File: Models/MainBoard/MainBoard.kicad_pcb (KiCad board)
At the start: 4 copper layers, 81 parts, among them J1 Conn_Coaxial, J10 Conn_01x04_Pin, J11 Conn_01x04_Pin, J12 Conn_01x04_Pin, J13 Conn_01x09_Pin, J14 Conn_01x13_Pin, J15 Conn_01x24_Socket, J18 Conn_01x24_Socket, J2 Conn_Coaxial, J3 Conn_Coaxial, J4 Conn_Coaxial, J5 Conn_Coaxial, J6 Conn_Coaxial, J7 Conn_01x04_Pin, J8 Conn_01x04_Pin, J9 Conn_01x04_Pin, U1 ADS8699, U2 AD7745, U3 DAC81404, U4 DAC81401, U5 ISO7761DW, U6 ISO1641DW

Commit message: Save progress
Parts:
- moved J2 23.4 mm to (70.8, 57.1)
- moved J1 12.3 mm to (53.5, 48.3)
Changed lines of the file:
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@@
 	(footprint "Connector_Custom:RFPC-SMA27-F"
 		(layer "F.Cu")
-		(at 53.98 60.66)
+		(at 53.48 48.34)
 		(property "Reference" "J1"
 			(at 0.415 -4.385 0)
@@
 			)
 		)
-		(property "Purchase Link" "https://www.digikey.com/en/products/detail/gct/RFPC-SMA27-F/22162144"
+		(property "Purchase Link" "https://www.digikey.com/en/products/detail/molex/0733660030/1465162"
 			(at 0 0 0)
 			(unlocked yes)
@@
 			)
 		)
-		(property "Cost" "$1.916"
+		(property "Cost" "$3.146"
 			(at 0 0 0)
 			(unlocked yes)
@@
 			)
 		)
-		(property "Purchase Link" "https://www.digikey.com/en/products/detail/gct/RFPC-SMA27-F/22162144"
+		(property "Purchase Link" "https://www.digikey.com/en/products/detail/molex/0733660030/1465162"
 			(at 0 0 0)
 			(unlocked yes)
@@
 			)
 		)
-		(property "Cost" "$1.916"
+		(property "Cost" "$3.146"
 			(at 0 0 0)
 			(unlocked yes)
@@
 			)
 		)
-		(property "Purchase Link" "https://www.digikey.com/en/products/detail/gct/RFPC-SMA27-F/22162144"
+		(property "Purchase Link" "https://www.digikey.com/en/products/detail/molex/0733660030/1465162"
 			(at 0 0 0)
 			(unlocked yes)
@@
 			)
 		)
-		(property "Cost" "$1.916"
+		(property "Cost" "$3.146"
 			(at 0 0 0)
 			(unlocked yes)
@@
 	(footprint "Connector_Custom:RFPC-SMA27-F"
 		(layer "F.Cu")
-		(at 53.98 73.36)
+		(at 70.78 57.08)
 		(property "Reference" "J2"
 			(at 0.415 -4.385 0)
@@
 			)
 		)
-		(property "Purchase Link" "https://www.digikey.com/en/products/detail/gct/RFPC-SMA27-F/22162144"
+		(property "Purchase Link" "https://www.digikey.com/en/products/detail/molex/0733660030/1465162"
 			(at 0 0 0)
 			(unlocked yes)
@@
 			)
 		)
-		(property "Cost" "$1.916"
+		(property "Cost" "$3.146"
 			(at 0 0 0)
 			(unlocked yes)
@@
 			)
 		)
-		(property "Purchase Link" "https://www.digikey.com/en/products/detail/gct/RFPC-SMA27-F/22162144"
+		(property "Purchase Link" "https://www.digikey.com/en/products/detail/molex/0733660030/1465162"
 			(at 0 0 0)
 			(unlocked yes)
@@
 			)
 		)
-		(property "Cost" "$1.916"
+		(property "Cost" "$3.146"
 			(at 0 0 0)
 			(unlocked yes)
@@
 			)
 		)
-		(property "Purchase Link" "https://www.digikey.com/en/products/detail/gct/RFPC-SMA27-F/22162144"
+		(property "Purchase Link" "https://www.digikey.com/en/products/detail/molex/0733660030/1465162"
 			(at 0 0 0)
 			(unlocked yes)
@@
 			)
 		)
-		(property "Cost" "$1.916"
+		(property "Cost" "$3.146"
 			(at 0 0 0)
 			(unlocked yes)

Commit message: Push uncommitted changes
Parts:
- J10, J11, J12, J7, J8, J9: value Conn_01x04_Pin -> Conn_01x03_Pin
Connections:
- J10 pad 3: /ADC_GND -> Net-(J10-Pin_3)
- J10 pad 4: Net-(J10-Pin_4) -> (no net)
- J11 pad 1: GND -> /CDC_EXC
- J11 pad 3: /CDC_EXC -> GND
- J11 pad 4: GND -> (no net)
- J12 pad 1: GND -> /CDC_CIN
- J12 pad 3: /CDC_CIN -> GND
- J12 pad 4: GND -> (no net)
- J7 pad 1: GND -> /BIAS_OUT
- J7 pad 3: /BIAS_OUT -> GND
- J7 pad 4: GND -> (no net)
- J8 pad 3: /BIAS_GND -> Net-(J8-Pin_3)
- J8 pad 4: Net-(J8-Pin_4) -> (no net)
- J9 pad 1: GND -> /ADC_IN
- J9 pad 3: /ADC_IN -> GND
- J9 pad 4: GND -> (no net)
- R1 pad 1: Net-(J8-Pin_4) -> Net-(J8-Pin_3)
- R2 pad 1: Net-(J10-Pin_4) -> Net-(J10-Pin_3)
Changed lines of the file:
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@@
 	(net 26 "/CDC_EXC")
 	(net 27 "/CDC_CIN")
-	(net 28 "Net-(J8-Pin_4)")
-	(net 29 "Net-(J10-Pin_4)")
+	(net 28 "Net-(J8-Pin_3)")
+	(net 29 "Net-(J10-Pin_3)")
 	(net 30 "15V")
 	(net 31 "-15V")
@@
 			)
 		)
-		(property "Value" "Conn_01x04_Pin"
+		(property "Value" "Conn_01x03_Pin"
 			(at -0.025 -4.965 90)
 			(unlocked yes)
@@
 			)
 		)
-		(property "Description" "Generic connector, single row, 01x04, script generated"
+		(property "Description" "Generic connector, single row, 01x03, script generated"
 			(at 0 0 90)
 			(unlocked yes)
@@
 			(layers "*.Cu" "*.Mask")
 			(remove_unused_layers no)
-			(net 1 "GND")
+			(net 24 "/ADC_IN")
 			(pinfunction "Pin_1")
 			(pintype "passive")
@@
 			(layers "*.Cu" "*.Mask")
 			(remove_unused_layers no)
-			(net 24 "/ADC_IN")
+			(net 1 "GND")
 			(pinfunction "Pin_3")
 			(pintype "passive")
@@
 			(layers "*.Cu" "*.Mask")
 			(remove_unused_layers no)
-			(net 1 "GND")
-			(pinfunction "Pin_4")
-			(pintype "passive")
 		)
 		(embedded_fonts no)
@@
 			)
 		)
-		(property "Value" "Conn_01x04_Pin"
+		(property "Value" "Conn_01x03_Pin"
 			(at -0.025 -4.965 90)
 			(unlocked yes)
@@
 			)
 		)
-		(property "Description" "Generic connector, single row, 01x04, script generated"
+		(property "Description" "Generic connector, single row, 01x03, script generated"
 			(at 0 0 90)
 			(unlocked yes)
@@
 			(layers "*.Cu" "*.Mask")
 			(remove_unused_layers no)
-			(net 1 "GND")
+			(net 26 "/CDC_EXC")
 			(pinfunction "Pin_1")
 			(pintype "passive")
@@
 			(layers "*.Cu" "*.Mask")
 			(remove_unused_layers no)
-			(net 26 "/CDC_EXC")
+			(net 1 "GND")
 			(pinfunction "Pin_3")
 			(pintype "passive")
@@
 			(layers "*.Cu" "*.Mask")
 			(remove_unused_layers no)
-			(net 1 "GND")
-			(pinfunction "Pin_4")
-			(pintype "passive")
 		)
 		(embedded_fonts no)
@@
 			(layers "F.Cu" "F.Mask" "F.Paste")
 			(roundrect_rratio 0.25)
-			(net 29 "Net-(J10-Pin_4)")
+			(net 29 "Net-(J10-Pin_3)")
 			(pintype "passive")
 			(thermal_bridge_angle 45)
@@
 			(layers "F.Cu" "F.Mask" "F.Paste")
 			(roundrect_rratio 0.25)
-			(net 28 "Net-(J8-Pin_4)")
+			(net 28 "Net-(J8-Pin_3)")
 			(pintype "passive")
 			(thermal_bridge_angle 45)
@@
 			)
 		)
-		(property "Value" "Conn_01x04_Pin"
+		(property "Value" "Conn_01x03_Pin"
 			(at -0.025 -4.965 90)
 			(unlocked yes)
@@
 			)
 		)
-		(property "Description" "Generic connector, single row, 01x04, script generated"
+		(property "Description" "Generic connector, single row, 01x03, script generated"
 			(at 0 0 90)
 			(unlocked yes)
@@
 			(layers "*.Cu" "*.Mask")
 			(remove_unused_layers no)
-			(net 1 "GND")
+			(net 27 "/CDC_CIN")
 			(pinfunction "Pin_1")
 			(pintype "passive")
@@
 			(layers "*.Cu" "*.Mask")
 			(remove_unused_layers no)
-			(net 27 "/CDC_CIN")
+			(net 1 "GND")
 			(pinfunction "Pin_3")
 			(pintype "passive")
@@
 			(layers "*.Cu" "*.Mask")
 			(remove_unused_layers no)
-			(net 1 "GND")
-			(pinfunction "Pin_4")
-			(pintype "passive")
 		)
 		(embedded_fonts no)
@@
 			)
 		)
-		(property "Value" "Conn_01x04_Pin"
+		(property "Value" "Conn_01x03_Pin"
 			(at -0.025 -4.965 90)
 			(unlocked yes)
@@
 			)
 		)
-		(property "Description" "Generic connector, single row, 01x04, script generated"
+		(property "Description" "Generic connector, single row, 01x03, script generated"
 			(at 0 0 90)
 			(unlocked yes)
@@
 			(layers "*.Cu" "*.Mask")
 			(remove_unused_layers no)
-			(net 1 "GND")
+			(net 22 "/BIAS_OUT")
 			(pinfunction "Pin_1")
 			(pintype "passive")
@@
 			(layers "*.Cu" "*.Mask")
 			(remove_unused_layers no)
-			(net 22 "/BIAS_OUT")
+			(net 1 "GND")
 			(pinfunction "Pin_3")
 			(pintype "passive")
@@
 			(layers "*.Cu" "*.Mask")
 			(remove_unused_layers no)
-			(net 1 "GND")
-			(pinfunction "Pin_4")
-			(pintype "passive")
 		)
 		(embedded_fonts no)
@@
 			)
 		)
-		(property "Value" "Conn_01x04_Pin"
+		(property "Value" "Conn_01x03_Pin"
 			(at -0.025 -4.965 90)
 			(unlocked yes)
@@
 			)
 		)
-		(property "Description" "Generic connector, single row, 01x04, script generated"
+		(property "Description" "Generic connector, single row, 01x03, script generated"
 			(at 0 0 90)
 			(unlocked yes)
@@
 			(layers "*.Cu" "*.Mask")
 			(remove_unused_layers no)
-			(net 25 "/ADC_GND")
+			(net 29 "Net-(J10-Pin_3)")
 			(pinfunction "Pin_3")
 			(pintype "passive")
@@
 			(layers "*.Cu" "*.Mask")
 			(remove_unused_layers no)
-			(net 29 "Net-(J10-Pin_4)")
-			(pinfunction "Pin_4")
-			(pintype "passive")
 		)
 		(embedded_fonts no)
@@
 			)
 		)
-		(property "Value" "Conn_01x04_Pin"
+		(property "Value" "Conn_01x03_Pin"
 			(at -0.025 -4.965 90)
 			(unlocked yes)
@@
 			)
 		)
-		(property "Description" "Generic connector, single row, 01x04, script generated"
+		(property "Description" "Generic connector, single row, 01x03, script generated"
 			(at 0 0 90)
 			(unlocked yes)
@@
 			(layers "*.Cu" "*.Mask")
 			(remove_unused_layers no)
-			(net 23 "/BIAS_GND")
+			(net 28 "Net-(J8-Pin_3)")
 			(pinfunction "Pin_3")
 			(pintype "passive")
@@
 			(layers "*.Cu" "*.Mask")
 			(remove_unused_layers no)
-			(net 28 "Net-(J8-Pin_4)")
-			(pinfunction "Pin_4")
-			(pintype "passive")
 		)
 		(embedded_fonts no)

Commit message: Save progress
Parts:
- removed J18: Conn_01x24_Socket, Connector_Custom:PinConnector_1x24
- added J16: Conn_01x24_Socket, Connector_Custom:PinConnector_1x24, F.Cu at (238.3, 81.8)
- added J19: Conn_01x24_Socket, Connector_Custom:PinConnector_1x24, F.Cu at (257.1, 81.6)
- J1, J2, J3, J4, J5, J6: footprint Connector_Custom:RFPC-SMA27-F -> Connector_Custom:Molex_MCX
- J10, J11, J12, J7, J8, J9: footprint Connector_Custom:PinConnector_1x4 -> Connector_Custom:PinConnector_1x3
- J13: value Conn_01x09_Pin -> Conn_01x02_Pin; footprint Connector_Custom:PinConnector_1x9 -> Connector_Custom:PinConnector_1x2
- J14: value Conn_01x13_Pin -> Conn_01x09_Pin; footprint Connector_Custom:PinConnector_1x13 -> Connector_Custom:PinConnector_1x9
- J15: value Conn_01x24_Socket -> Conn_01x13_Pin; footprint Connector_Custom:PinConnector_1x24 -> Connector_Custom:PinConnector_1x13
- moved J14 146.3 mm to (128.6, 169.3)
- moved J13 123.6 mm to (247.1, 155.1)
- moved J15 113.8 mm to (129.1, 18.4), turned to 90 degrees
- moved C5 36.9 mm to (138.5, 123.9)
- moved C4 32.5 mm to (138.8, 126.4)
- moved C3 32.0 mm to (133.2, 124.0), turned to 180 degrees
- moved NT2 30.9 mm to (139.9, 122.2), turned to 90 degrees
- moved R5 30.9 mm to (165.4, 127.5), turned to 180 degrees
- moved C1 30.2 mm to (129.5, 127.4), turned to 90 degrees
- moved R3 30.1 mm to (138.0, 134.8), turned to 180 degrees
- moved U1 29.6 mm to (135.6, 130.5)
- moved C10 28.6 mm to (162.3, 64.7)
- moved C9 28.2 mm to (168.7, 132.1), turned to 90 degrees
- moved NT3 27.7 mm to (170.5, 131.0)
- moved C2 27.1 mm to (133.0, 126.4), turned to 180 degrees
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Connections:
- J13 pad 2: 15V -> GND
- J14 pad 2: /SENSENA -> 15V
- J14 pad 3: /OUTA -> GND
- J14 pad 4: GND -> -15V
- J14 pad 5: /SENSENB -> GND
- J14 pad 6: /OUTB -> 5V
- J14 pad 8: /SENSENC -> 3.3V
- J14 pad 9: /OUTC -> GND
- J15 pad 1: unconnected-(J15-Pin_1-Pad1) -> GND
- J15 pad 10: /Isolation/GND_Digital -> GND
- J15 pad 11: /Isolation/SCK_Digital -> /SENSEND
- J15 pad 12: unconnected-(J15-Pin_12-Pad12) -> /OUTD
- J15 pad 13: unconnected-(J15-Pin_13-Pad13) -> GND
- J15 pad 2: unconnected-(J15-Pin_2-Pad2) -> /SENSENA
- J15 pad 3: unconnected-(J15-Pin_3-Pad3) -> /OUTA
- J15 pad 4: /Isolation/CS1_Digital -> GND
- J15 pad 5: /Isolation/CS2_Digital -> /SENSENB
- J15 pad 6: unconnected-(J15-Pin_6-Pad6) -> /OUTB
- J15 pad 7: unconnected-(J15-Pin_7-Pad7) -> GND
- J15 pad 8: unconnected-(J15-Pin_8-Pad8) -> /SENSENC
- J15 pad 9: unconnected-(J15-Pin_9-Pad9) -> /OUTC
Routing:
- net GND: vias 0 -> 3
- added copper zone on F.Cu, net GND

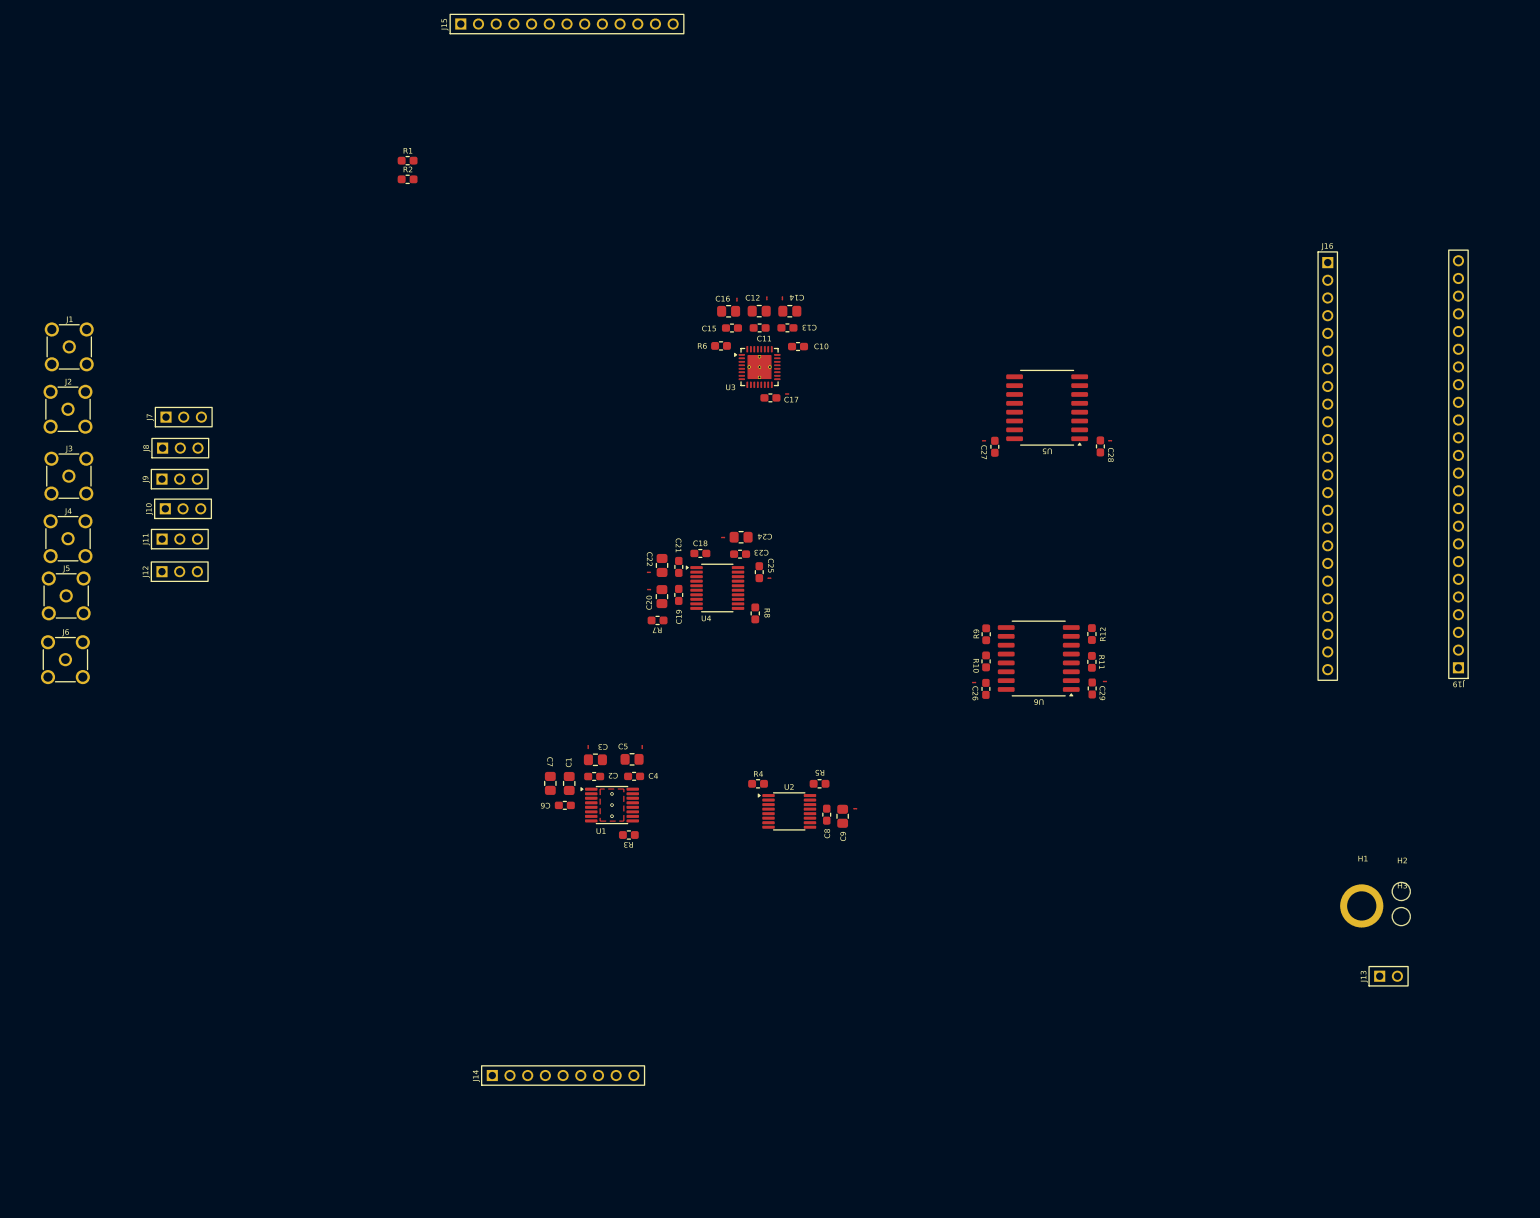
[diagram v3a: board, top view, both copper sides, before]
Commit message: Everything is now aligned very well on the power board
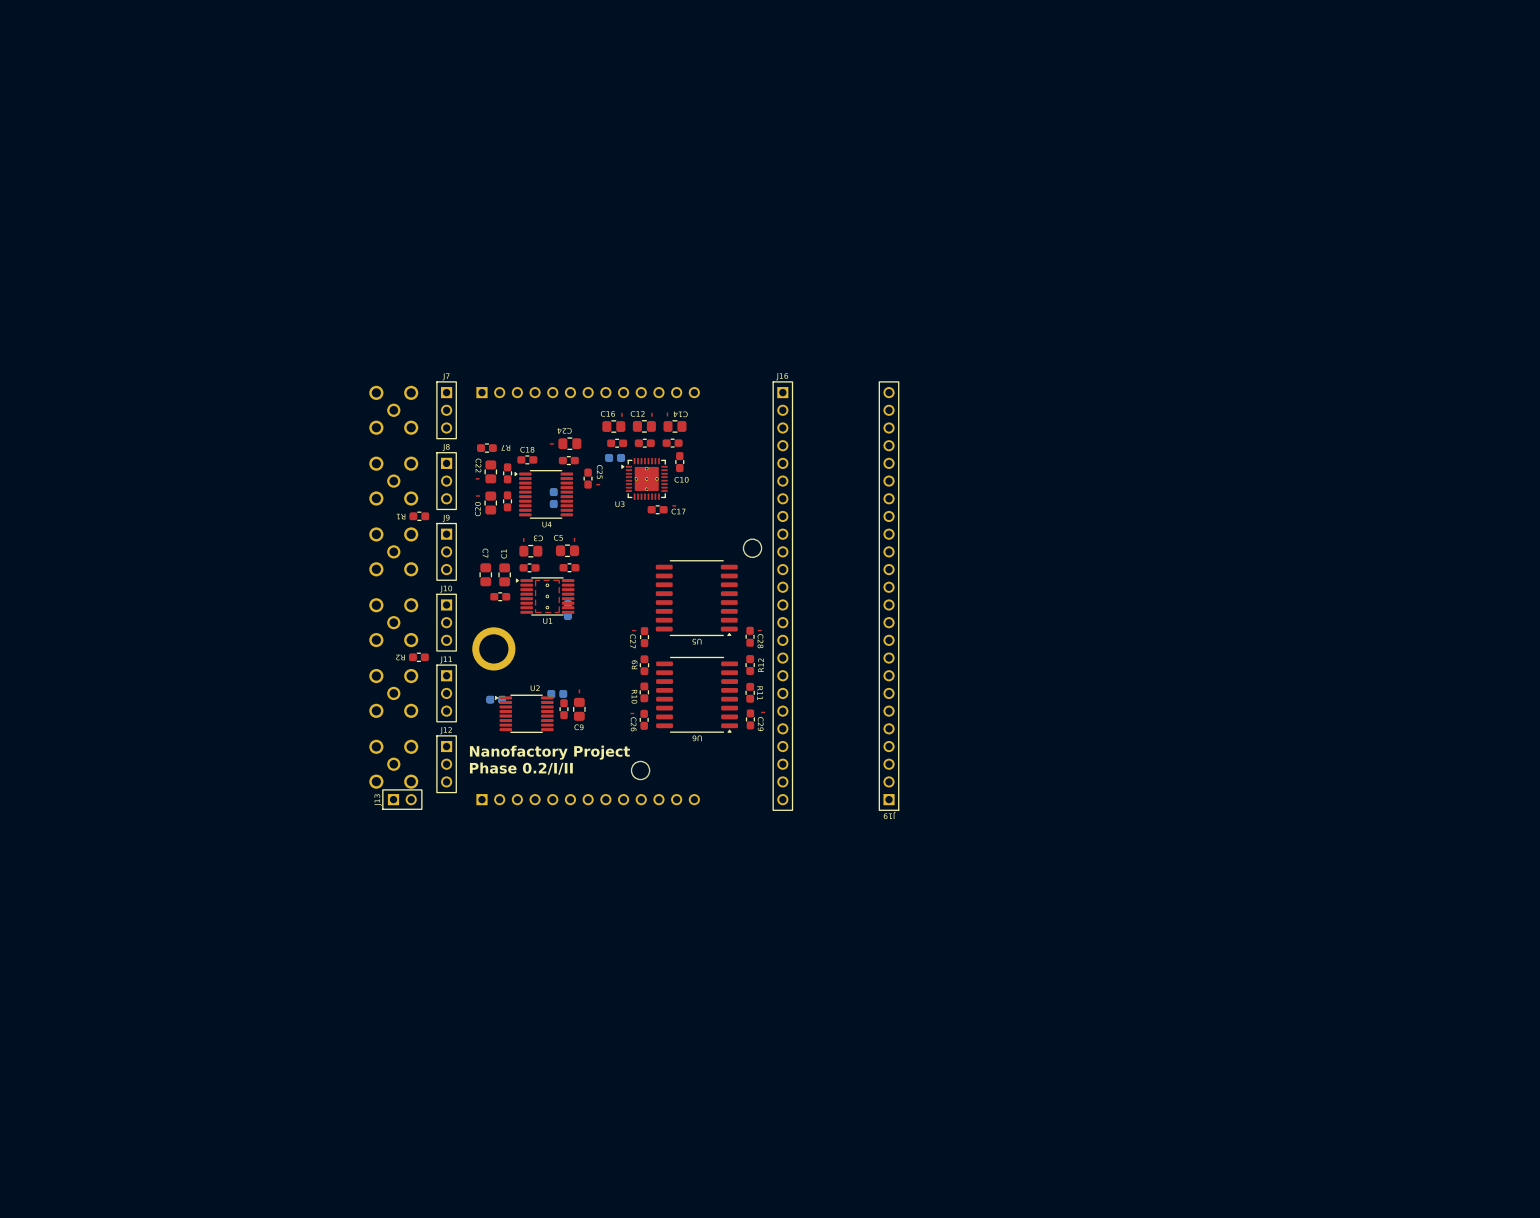
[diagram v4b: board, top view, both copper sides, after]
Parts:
- J1, J15, J2, J3, J4, J5, J6, R3, R4, R5, R6, R8: moved to B.Cu
- J14: value Conn_01x09_Pin -> Conn_01x13_Pin; footprint Connector_Custom:PinConnector_1x9 -> Connector_Custom:PinConnector_1x13; moved to B.Cu
- moved J13 143.8 mm to (105.5, 129.7)
- moved H1 129.9 mm to (118.6, 108.1)
- moved H3 111.2 mm to (139.7, 125.5)
- moved H2 105.3 mm to (155.8, 93.6)
- moved J19 83.9 mm to (175.4, 100.5)
- moved J16 80.4 mm to (160.1, 100.5)
- moved R2 68.6 mm to (107.9, 109.3), turned to 180 degrees
- moved U5 57.2 mm to (147.8, 100.8)
- moved C27 57.2 mm to (140.3, 106.4)
- moved C28 57.2 mm to (155.4, 106.3)
- moved NT14 57.2 mm to (156.8, 105.5)
- moved NT13 57.1 mm to (138.8, 105.5)
- moved J15 53.0 mm to (132.2, 71.3), turned to -90 degrees
- moved R1 51.1 mm to (108.0, 89.0), turned to 180 degrees
- moved J6 49.5 mm to (104.3, 124.6)
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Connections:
- J14 pad 2: 15V -> -15V
- J14 pad 4: -15V -> 15V
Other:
- board text added: "Nanofactory Project Phase 0.2/I/II"
